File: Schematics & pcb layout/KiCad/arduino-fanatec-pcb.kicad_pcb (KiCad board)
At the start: 2 copper layers, 71.1 x 80 mm, 20 parts, among them J1 SPI Connector 01x08_Male, J1.2 Extra pin breakout, J2 TM1637 4 digit Display connec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, J3 Breakout Connector 02x18_Odd_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, U1 Simple_Chinese_Logic_level_sh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

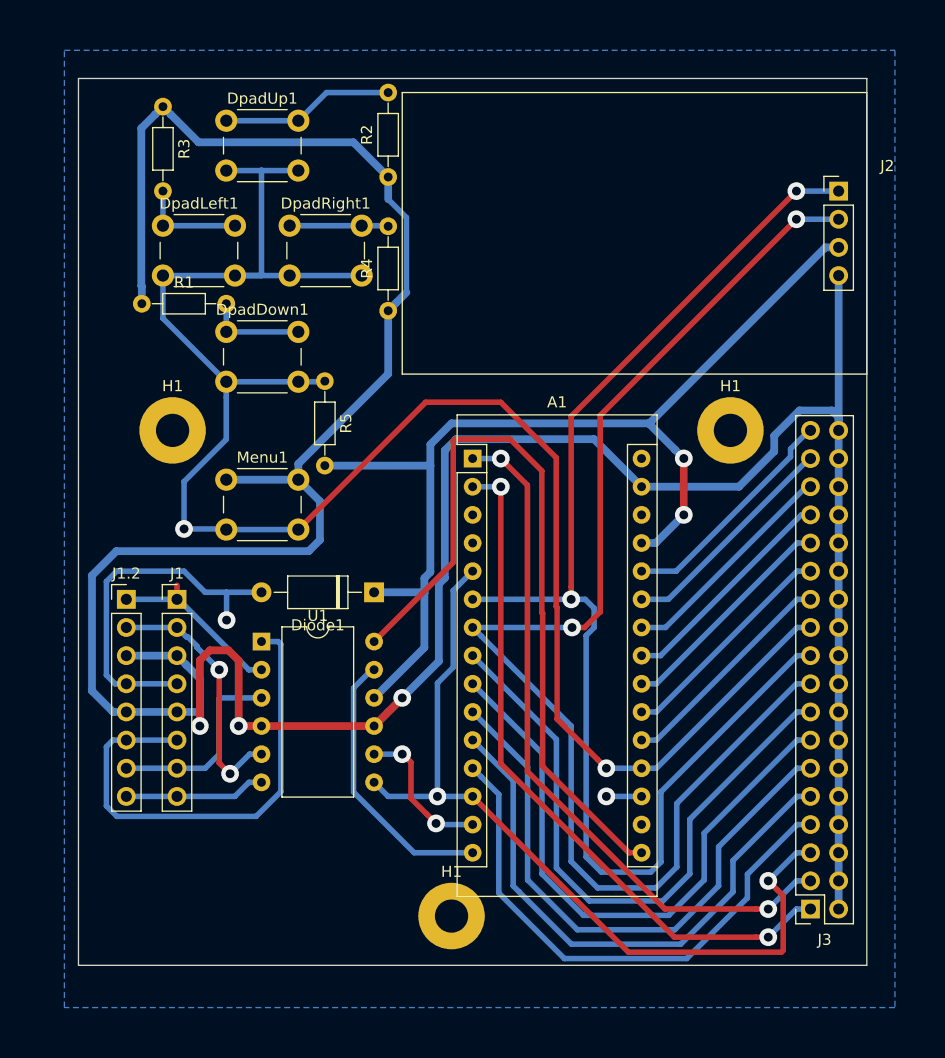
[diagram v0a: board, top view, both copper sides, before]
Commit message: Updated the PCB front silkscreen, exported Geber files for manufacturing according to jlcpcb's requirements
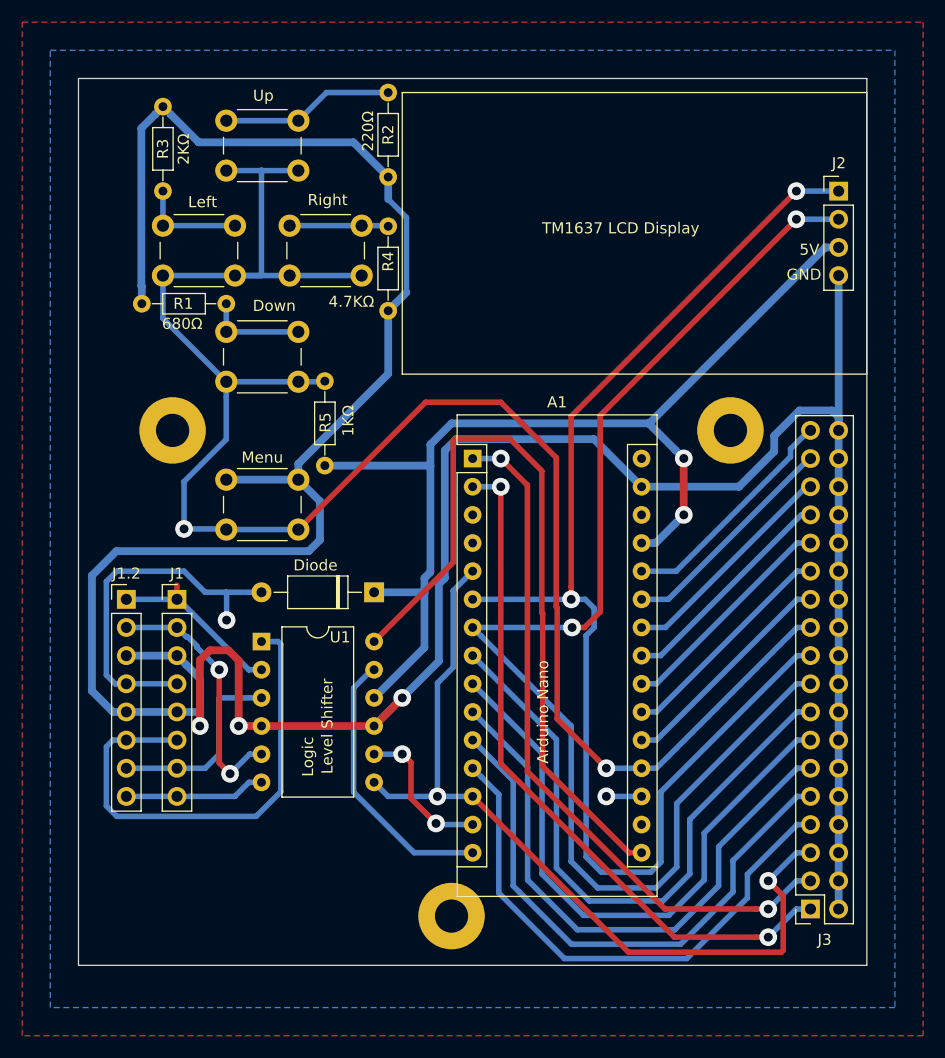
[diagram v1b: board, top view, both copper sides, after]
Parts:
- removed DpadDown1, DpadUp1: SW_Push, Button_Switch_THT:SW_PUSH_6mm
- added Down: SW_Push, Button_Switch_THT:SW_PUSH_6mm, F.Cu at (64.1, 58.4)
- added Up: SW_Push, Button_Switch_THT:SW_PUSH_6mm, F.Cu at (64.1, 39.4)
- Level Shifter: renamed from U1
- renumbered Diode1 to Diode, DpadLeft1 to Left, Menu1 to Menu, DpadRight1 to Right
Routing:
- added copper zone on F.Cu, net GND
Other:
- board text added: "1KΩ"
- board text added: "220Ω"
- board text added: "2KΩ"
- board text added: "4.7KΩ"
- board text added: "5V"
- board text added: "680Ω"
- board text added: "Arduino Nano"
- board text added: "GND"
- board text added: "Logic"
- board text added: "TM1637 LCD Display"
- board text added: "U1"
